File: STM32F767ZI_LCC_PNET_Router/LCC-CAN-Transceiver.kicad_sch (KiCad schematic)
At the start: 18 parts, among them J201 Termination, J202 RJ45, J203 RJ45, T201 LCC Power Out, T202 LCC Power In, U201 LM358, U202 TCAN332DR

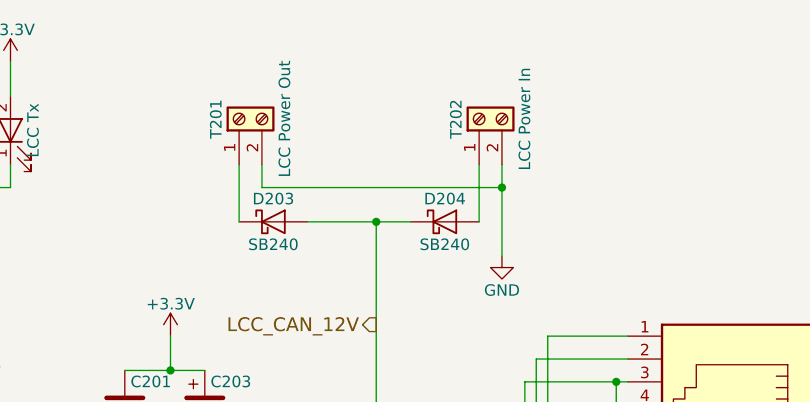
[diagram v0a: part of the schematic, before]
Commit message: Add plus signs to power terminal marking (show polarity).
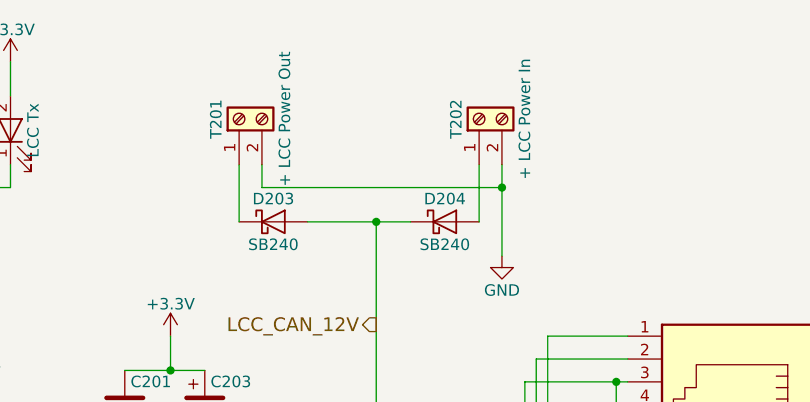
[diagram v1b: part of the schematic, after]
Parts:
- T201: value LCC Power Out -> + LCC Power Out
- T202: value LCC Power In -> + LCC Power In
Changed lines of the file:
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@@
     (in_bom yes) (on_board yes)
     (property "Reference" "T201" (id 0) (at 143.51 30.48 0))
-    (property "Value" "LCC Power Out" (id 1) (at 151.13 30.48 0))
+    (property "Value" "+ LCC Power Out" (id 1) (at 151.13 30.48 0))
     (property "Footprint" "TerminalBlock_TE-Connectivity:TerminalBlock_TE_282834-2_1x02_P2.54mm_Horizontal" (id 2) (at 146.05 30.48 0)
       (effects (font (size 1.27 1.27)) hide)
@@
     (in_bom yes) (on_board yes)
     (property "Reference" "T202" (id 0) (at 170.18 30.48 0))
-    (property "Value" "LCC Power In" (id 1) (at 177.8 30.48 0))
+    (property "Value" "+ LCC Power In" (id 1) (at 177.8 30.48 0))
     (property "Footprint" "TerminalBlock_TE-Connectivity:TerminalBlock_TE_282834-2_1x02_P2.54mm_Horizontal" (id 2) (at 172.72 30.48 0)
       (effects (font (size 1.27 1.27)) hide)
